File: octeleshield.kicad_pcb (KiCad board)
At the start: 2 copper layers, 30 parts, among them P1 POWER_HEADER, P10 THERMOCOUPLE1, P11 THERMOCOUPLE2, P2 ANALOG_HEADER, P3 ICSP_HEADER, P4 DIGITAL_HEADER_2, P5 DIGITAL_HEADER_1, P6 V_PROBE2_SIG, P7 V_PROBE2_GND, P8 V_PROBE1_SIG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

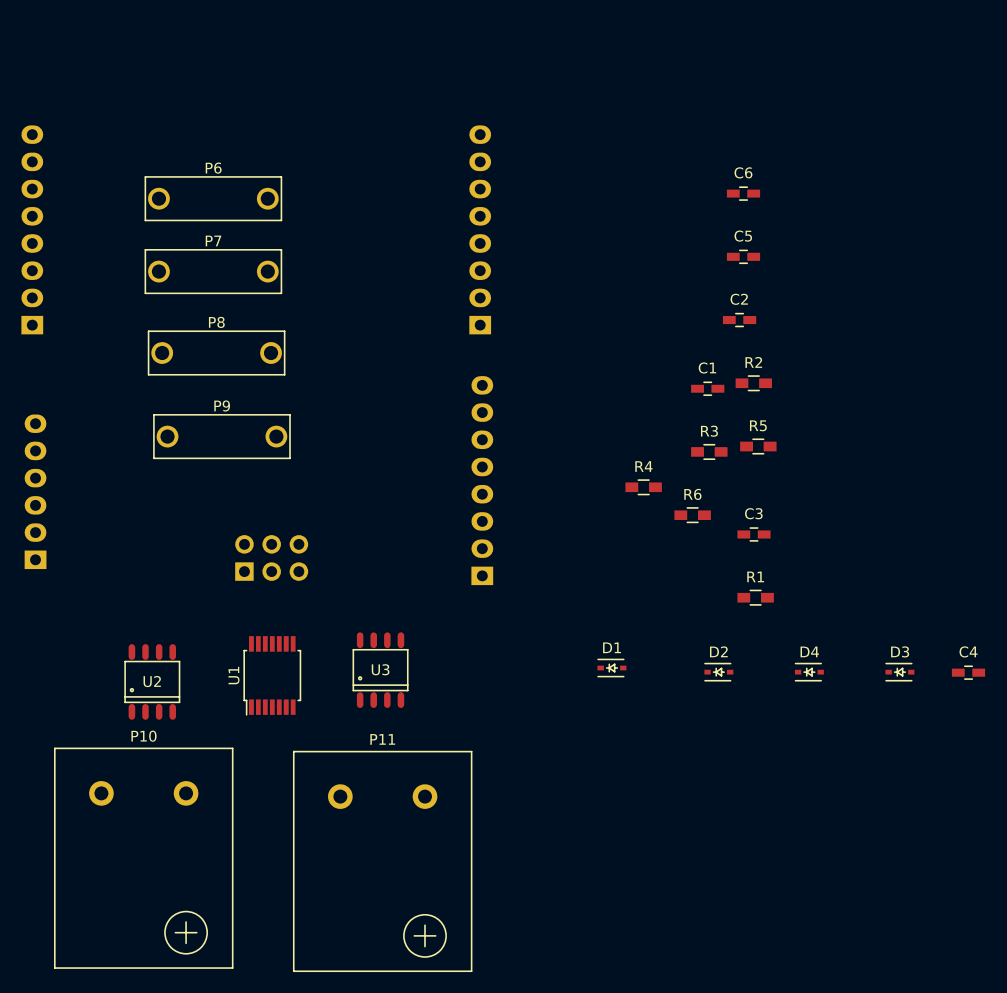
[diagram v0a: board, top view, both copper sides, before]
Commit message: work in progress, first try of pcb layout
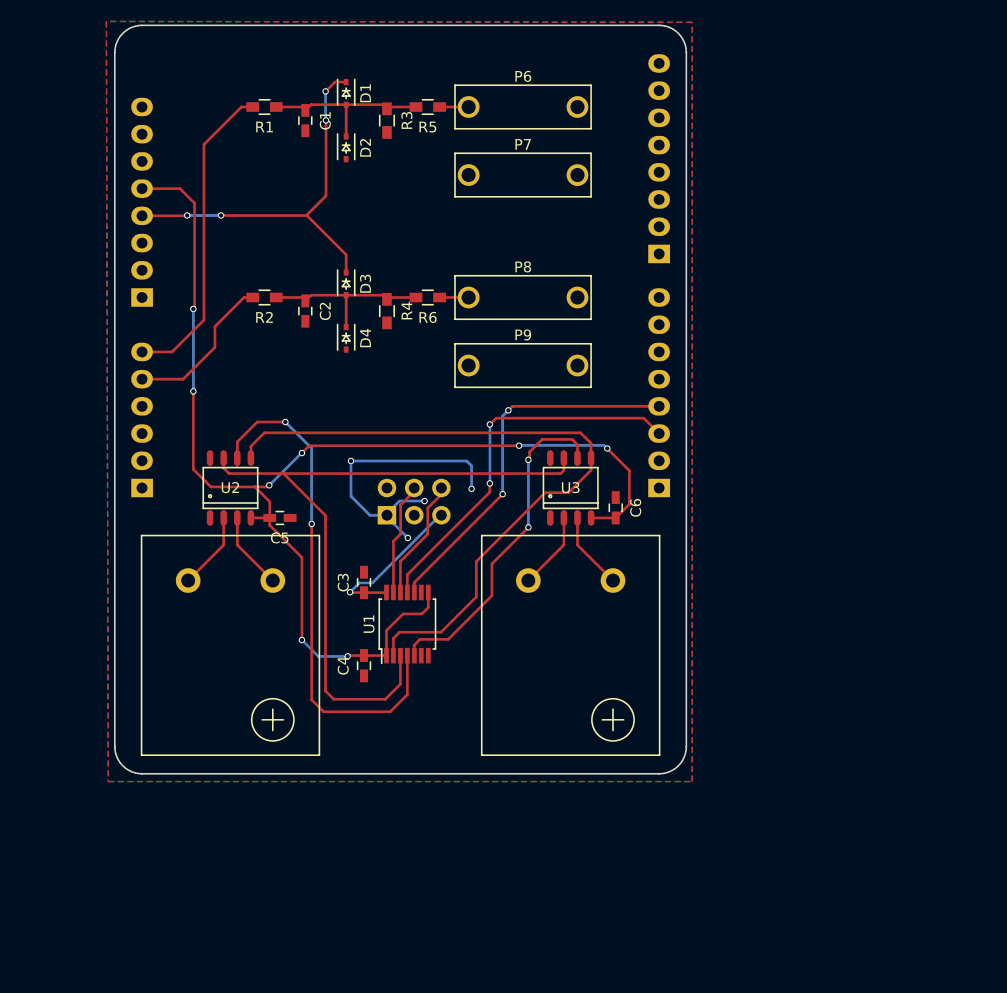
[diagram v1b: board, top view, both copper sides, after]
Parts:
- moved R1 64.8 mm to (115.6, 66.0), turned to 180 degrees
- moved D3 63.1 mm to (123.2, 82.5), turned to 270 degrees
- moved D2 60.0 mm to (123.2, 69.8), turned to 270 degrees
- moved D1 59.1 mm to (123.2, 64.8), turned to 270 degrees
- moved C4 56.4 mm to (124.9, 118.2), turned to 90 degrees
- moved D4 53.3 mm to (123.2, 87.6), turned to 270 degrees
- moved C5 49.7 mm to (117.0, 104.4), turned to 180 degrees
- moved R2 46.4 mm to (115.6, 83.8), turned to 180 degrees
- moved C1 45.1 mm to (119.4, 67.3), turned to 270 degrees
- moved R5 44.2 mm to (130.8, 66.0), turned to 180 degrees
- moved R3 43.1 mm to (127.0, 67.3), turned to 270 degrees
- moved C2 40.5 mm to (119.4, 85.1), turned to 270 degrees
- moved C3 36.7 mm to (124.9, 110.4), turned to 90 degrees
- moved R6 32.0 mm to (130.8, 83.8), turned to 180 degrees
- moved C6 31.7 mm to (148.4, 103.4), turned to 270 degrees
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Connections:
- P2 pad 1: /A0 -> Net-(P2-Pad1)
- P2 pad 2: /A1 -> Net-(P2-Pad2)
- P2 pad 5: Net-(P2-Pad5) -> /A4
- P2 pad 6: Net-(P2-Pad6) -> /A5
- P5 pad 3: Net-(P5-Pad3) -> /CS1
- P5 pad 4: Net-(P5-Pad4) -> /CS2
- P5 pad 5: /TC_ENABLE -> Net-(P5-Pad5)
- P5 pad 6: /CS1 -> Net-(P5-Pad6)
- P5 pad 7: /CS2 -> Net-(P5-Pad7)
- R1 pad 2: /A1 -> /A5
- R2 pad 2: /A0 -> /A4
- U1 pad 8: /TC_ENABLE -> +3V3
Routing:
- net +3V3: track 0.00 -> 116.5 mm, vias 0 -> 8
- net Net-(U1-Pad3): track 0.00 -> 66.6 mm
- net Net-(U1-Pad2): track 0.00 -> 64.8 mm
- net +5V: track 0.00 -> 51.8 mm, vias 0 -> 5
- net Net-(U1-Pad4): track 0.00 -> 48.1 mm, vias 0 -> 2
- net /CS1: track 0.00 -> 35.5 mm, vias 0 -> 2
- net /CS2: track 0.00 -> 34.9 mm, vias 0 -> 2
- net Net-(U1-Pad5): track 0.00 -> 31.4 mm, vias 0 -> 2
- net /A5: track 0.00 -> 29.4 mm
- net GND: track 0.00 -> 28.1 mm, vias 0 -> 4
- net Net-(C2-Pad1): track 0.00 -> 16.6 mm
- net Net-(C1-Pad1): track 0.00 -> 16.6 mm
- net /A4: track 0.00 -> 14.6 mm
- net /MISO: track 0.00 -> 12.6 mm
- net /SCLK: track 0.00 -> 11.1 mm
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- added copper zone on B.Cu, net GND
- added copper zone on F.Cu, net GND
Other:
- board outline added: 53.3 x 69.9 mm

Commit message: work in progress, component updates
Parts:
- C1, C2: value 10n -> 100n
- C3, C4, C5, C6: value 0.1u -> 100n
- R5, R6: value 33.2k -> 33k
- U2, U3: value MAX31855KASA -> MAX31855KASA+
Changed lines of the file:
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@@
-(kicad_pcb (version 4) (host pcbnew 4.0.1-stable)
+(kicad_pcb (version 4) (host pcbnew 4.0.2-stable)
   (general
     (links 57)
@@
   (title_block
     (title "Overclocking telemetry shield for Arduino Yún")
-    (date 2016-01-17)
+    (date 2016-02-22)
     (rev v1)
     (company Moonpunch.org)
@@
       (effects (font (size 1 1) (thickness 0.15)))
     )
-    (fp_text value 10n (at 0 1.9 270) (layer F.Fab)
+    (fp_text value 100n (at 0 1.9 270) (layer F.Fab)
       (effects (font (size 1 1) (thickness 0.15)))
     )
@@
       (effects (font (size 1 1) (thickness 0.15)))
     )
-    (fp_text value 10n (at 0 1.9 270) (layer F.Fab)
+    (fp_text value 100n (at 0 1.9 270) (layer F.Fab)
       (effects (font (size 1 1) (thickness 0.15)))
     )
@@
       (effects (font (size 1 1) (thickness 0.15)))
     )
-    (fp_text value 0.1u (at 0 1.9 90) (layer F.Fab)
+    (fp_text value 100n (at 0 1.9 90) (layer F.Fab)
       (effects (font (size 1 1) (thickness 0.15)))
     )
@@
       (effects (font (size 1 1) (thickness 0.15)))
     )
-    (fp_text value 0.1u (at 0 1.9 90) (layer F.Fab)
+    (fp_text value 100n (at 0 1.9 90) (layer F.Fab)
       (effects (font (size 1 1) (thickness 0.15)))
     )
@@
       (effects (font (size 1 1) (thickness 0.15)))
     )
-    (fp_text value 0.1u (at 0 1.9 180) (layer F.Fab)
+    (fp_text value 100n (at 0 1.9 180) (layer F.Fab)
       (effects (font (size 1 1) (thickness 0.15)))
     )
@@
       (effects (font (size 1 1) (thickness 0.15)))
     )
-    (fp_text value 0.1u (at 0 1.9 270) (layer F.Fab)
+    (fp_text value 100n (at 0 1.9 270) (layer F.Fab)
       (effects (font (size 1 1) (thickness 0.15)))
     )
@@
       (effects (font (size 1 1) (thickness 0.15)))
     )
-    (fp_text value 33.2k (at 0 1.9 180) (layer F.Fab)
+    (fp_text value 33k (at 0 1.9 180) (layer F.Fab)
       (effects (font (size 1 1) (thickness 0.15)))
     )
@@
       (effects (font (size 1 1) (thickness 0.15)))
     )
-    (fp_text value 33.2k (at 0 1.9 180) (layer F.Fab)
+    (fp_text value 33k (at 0 1.9 180) (layer F.Fab)
       (effects (font (size 1 1) (thickness 0.15)))
     )
@@
       (effects (font (size 1 1) (thickness 0.15)))
     )
-    (fp_text value MAX31855KASA (at 0 0) (layer F.Fab)
+    (fp_text value MAX31855KASA+ (at 0 0) (layer F.Fab)
       (effects (font (size 1 1) (thickness 0.15)))
     )
@@
       (effects (font (size 1 1) (thickness 0.15)))
     )
-    (fp_text value MAX31855KASA (at 0 0) (layer F.Fab)
+    (fp_text value MAX31855KASA+ (at 0 0) (layer F.Fab)
       (effects (font (size 1 1) (thickness 0.15)))
     )
@@
       (effects (font (size 1 1) (thickness 0.15)))
     )
-    (fp_text value THERMOCOUPLE1 (at 0.05 17.3) (layer F.Fab)
+    (fp_text value THERMOCOUPLE1 (at 0.05 17.3) (layer F.SilkS)
       (effects (font (size 1 1) (thickness 0.15)))
     )
@@
       (effects (font (size 1 1) (thickness 0.15)))
     )
-    (fp_text value THERMOCOUPLE2 (at 0.05 17.3) (layer F.Fab)
-      (effects (font (size 1 1) (thickness 0.15)))
-    )
+    (fp_text value THERMOCOUPLE2 (at 0.05 17.3) (layer F.SilkS)
+      (effects (font (size 1 1) (thickness 0.15)))
+    )

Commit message: more work in progress, getting there
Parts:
- added G***: MOONPUNCH_LOGO, parts:moonpunch_1cm, F.Cu at (108.5, 61.5)
- added G***: LOGO, parts:epeak_logo, F.Cu at (122.8, 95.1)
- P10: value THERMOCOUPLE1 -> THERMOCOUPLE1/D3
- P11: value THERMOCOUPLE2 -> THERMOCOUPLE2/D4
- P6: value V_PROBE2_SIG -> V_PROBE1_SIG
- P7: value V_PROBE2_GND -> V_PROBE1_GND
- P8: value V_PROBE1_SIG -> V_PROBE2_SIG
- P9: value V_PROBE1_GND -> V_PROBE2_GND
- U2, U3: value MAX31855KASA+ -> MAX31855
- moved P10 1.00 mm to (112.4, 111.2)
- moved P11 1.00 mm to (144.1, 111.2)
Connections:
- net /A4 renamed /A1
- net /A5 renamed /A0
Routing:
- net Net-(P11-Pad2): track 7.22 -> 8.22 mm
- net Net-(P11-Pad1): track 7.22 -> 8.22 mm
- net Net-(P10-Pad1): track 7.22 -> 8.22 mm
- net Net-(P10-Pad2): track 7.22 -> 8.22 mm
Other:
- board text added: "Designed in Taiwan 2016-02-24"
- board text added: "EPEAK GEARS"
- board text added: "Overclocking Telemetry Shield"
- board text added: "Voltage1/A0"
- board text added: "Voltage2/A1"
- board text added: "moonpunch.org"
- board text added: "v1"

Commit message: PCB modifications
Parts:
- moved C6 1.43 mm to (149.5, 104.4), turned to 180 degrees
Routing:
- net +3V3: track 116.5 -> 115.5 mm
- net Net-(U1-Pad4): track 48.1 -> 49.1 mm
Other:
- board text added: "Designed in Taiwan 2016-03-01"
- board text added: "rev0"
- board text removed: "Designed in Taiwan 2016-02-24"
- board text removed: "v1"
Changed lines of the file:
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@@
     (visible_elements FFFFE77F)
     (pcbplotparams
-      (layerselection 0x020f0_80000001)
-      (usegerberextensions false)
+      (layerselection 0x010f0_80000001)
+      (usegerberextensions true)
       (excludeedgelayer true)
       (linewidth 0.100000)
@@
   )
   (module Capacitors_SMD:C_0603_HandSoldering (layer F.Cu)
-    (at 148.35124 103.44404 270)
+    (at 149.45106 104.3559 180)
     (descr "Capacitor SMD 0603, hand soldering")
     (tags "capacitor 0603")
     (attr smd)
-    (fp_text reference C6 (at 1.27508 -1.68656 270) (layer F.SilkS)
-      (effects (font (size 1 1) (thickness 0.15)))
-    )
-    (fp_text value 100n (at -2.35712 -1.68656 270) (layer F.SilkS)
+    (fp_text reference C6 (at 1.00584 1.397 180) (layer F.SilkS)
+      (effects (font (size 1 1) (thickness 0.15)))
+    )
+    (fp_text value 100n (at 0.11176 -1.397 180) (layer F.SilkS)
       (effects (font (size 1 1) (thickness 0.15)))
     )
@@
     (fp_line (start -0.35 -0.6) (end 0.35 -0.6) (layer F.SilkS) (width 0.15))
     (fp_line (start 0.35 0.6) (end -0.35 0.6) (layer F.SilkS) (width 0.15))
-    (pad 1 smd rect (at -0.95 0 270) (size 1.2 0.75) (layers F.Cu F.Paste F.Mask)
+    (pad 1 smd rect (at -0.95 0 180) (size 1.2 0.75) (layers F.Cu F.Paste F.Mask)
       (net 2 GND))
-    (pad 2 smd rect (at 0.95 0 270) (size 1.2 0.75) (layers F.Cu F.Paste F.Mask)
+    (pad 2 smd rect (at 0.95 0 180) (size 1.2 0.75) (layers F.Cu F.Paste F.Mask)
       (net 5 +3V3))
     (model Capacitors_SMD.3dshapes/C_0603_HandSoldering.wrl
@@
     (pad "" np_thru_hole circle (at 0 10.25) (size 2.6 2.6) (drill 2.6) (layers *.Cu *.Mask F.SilkS))
   )
-  (gr_text "Designed in Taiwan\n2016-02-24" (at 114.554 62.25032) (layer B.SilkS)
+  (gr_text "Designed in Taiwan\n2016-03-01" (at 114.554 62.25032) (layer B.SilkS)
     (effects (font (size 1.5 1.5) (thickness 0.3)) (justify mirror))
   )
-  (gr_text v1 (at 133.60908 126.67996) (layer F.SilkS)
+  (gr_text rev0 (at 133.79704 126.7714) (layer F.SilkS)
     (effects (font (size 1.016 1.016) (thickness 0.1524)))
   )
@@
   (segment (start 126.9412 111.3638) (end 126.955 111.35) (width 0.25) (layer F.Cu) (net 4))
   (segment (start 132.08 104.14) (end 132.06476 104.14) (width 0.25) (layer B.Cu) (net 4))
+  (segment (start 148.3512 104.394) (end 148.35124 104.39404) (width 0.25) (layer F.Cu) (net 5))
+  (via (at 147.56384 97.917) (size 0.6) (drill 0.4) (layers F.Cu B.Cu) (net 5))
+  (segment (start 147.56384 97.917) (end 148.39188 98.74504) (width 0.25) (layer F.Cu) (net 5))
+  (segment (start 148.39188 98.74504) (end 148.39188 104.3534) (width 0.25) (layer F.Cu) (net 5))
+  (segment (start 148.39188 104.3534) (end 148.35124 104.39404) (width 0.25) (layer F.Cu) (net 5))
+  (segment (start 147.25904 97.6122) (end 147.56384 97.917) (width 0.25) (layer B.Cu) (net 5))
+  (segment (start 119.75084 97.65284) (end 139.33424 97.65284) (width 0.25) (layer F.Cu) (net 5))
+  (via (at 139.33424 97.65284) (size 0.6) (drill 0.4) (layers F.Cu B.Cu) (net 5))
+  (segment (start 139.33424 97.65284) (end 139.37488 97.6122) (width 0.25) (layer B.Cu) (net 5))
+  (segment (start 139.37488 97.6122) (end 147.25904 97.6122) (width 0.25) (layer B.Cu) (net 5))
   (segment (start 114.681 101.4984) (end 115.86464 101.4984) (width 0.25) (layer F.Cu) (net 5))
-  (segment (start 149.62124 103.12404) (end 148.35124 104.39404) (width 0.25) (layer F.Cu) (net 5))
-  (segment (start 149.62124 99.9744) (end 149.62124 103.12404) (width 0.25) (layer F.Cu) (net 5))
-  (segment (start 147.56384 97.917) (end 149.62124 99.9744) (width 0.25) (layer F.Cu) (net 5))
-  (via (at 147.56384 97.917) (size 0.6) (drill 0.4) (layers F.Cu B.Cu) (net 5))
-  (segment (start 147.25904 97.6122) (end 147.56384 97.917) (width 0.25) (layer B.Cu) (net 5))
-  (segment (start 139.37488 97.6122) (end 147.25904 97.6122) (width 0.25) (layer B.Cu) (net 5))
-  (segment (start 139.33424 97.65284) (end 139.37488 97.6122) (width 0.25) (layer B.Cu) (net 5))
-  (via (at 139.33424 97.65284) (size 0.6) (drill 0.4) (layers F.Cu B.Cu) (net 5))
-  (segment (start 119.75084 97.65284) (end 139.33424 97.65284) (width 0.25) (layer F.Cu) (net 5))
+  (segment (start 146.05 104.394) (end 148.3512 104.394) (width 0.25) (layer F.Cu) (net 5))
+  (segment (start 115.86464 101.4984) (end 116.01704 101.346) (width 0.25) (layer F.Cu) (net 5))
+  (via (at 116.01704 101.346) (size 0.6) (drill 0.4) (layers F.Cu B.Cu) (net 5))
+  (segment (start 116.01704 101.346) (end 119.0244 98.33864) (width 0.25) (layer B.Cu) (net 5))
+  (segment (start 119.0244 98.33864) (end 119.06504 98.33864) (width 0.25) (layer B.Cu) (net 5))
+  (via (at 119.06504 98.33864) (size 0.6) (drill 0.4) (layers F.Cu B.Cu) (net 5))
   (segment (start 119.06504 98.33864) (end 119.75084 97.65284) (width 0.25) (layer F.Cu) (net 5))
-  (via (at 119.06504 98.33864) (size 0.6) (drill 0.4) (layers F.Cu B.Cu) (net 5))
-  (segment (start 119.0244 98.33864) (end 119.06504 98.33864) (width 0.25) (layer B.Cu) (net 5))
-  (segment (start 116.01704 101.346) (end 119.0244 98.33864) (width 0.25) (layer B.Cu) (net 5))
-  (via (at 116.01704 101.346) (size 0.6) (drill 0.4) (layers F.Cu B.Cu) (net 5))
-  (segment (start 115.86464 101.4984) (end 116.01704 101.346) (width 0.25) (layer F.Cu) (net 5))
   (segment (start 116.05764 104.394) (end 116.05764 105.08484) (width 0.25) (layer F.Cu) (net 5))
   (segment (start 123.40848 117.2362) (end 124.85624 117.2362) (width 0.25) (layer F.Cu) (net 5))
@@
   (segment (start 114.681 101.4984) (end 110.5662 101.4984) (width 0.25) (layer F.Cu) (net 5))
   (segment (start 116.05764 102.87504) (end 114.681 101.4984) (width 0.25) (layer F.Cu) (net 5))
-  (segment (start 146.05 104.394) (end 148.3512 104.394) (width 0.25) (layer F.Cu) (net 5))
-  (segment (start 148.3512 104.394) (end 148.35124 104.39404) (width 0.25) (layer F.Cu) (net 5))
   (segment (start 126.955 117.25) (end 126.955 114.9038) (width 0.25) (layer F.Cu) (net 5))
   (segment (start 130.855 112.7564) (end 130.855 111.35) (width 0.25) (layer F.Cu) (net 5))
@@
   (segment (start 146.05 98.806) (end 146.05 99.93376) (width 0.25) (layer F.Cu) (net 34))
   (segment (start 127.605 115.64064) (end 127.605 117.25) (width 0.25) (layer F.Cu) (net 34))
-  (segment (start 128.18872 115.05692) (end 127.605 115.64064) (width 0.25) (layer F.Cu) (net 34))
-  (segment (start 132.04444 115.05692) (end 128.18872 115.05692) (width 0.25) (layer F.Cu) (net 34))
-  (segment (start 135.34136 111.76) (end 132.04444 115.05692) (width 0.25) (layer F.Cu) (net 34))
-  (segment (start 135.34136 108.46308) (end 135.34136 111.76) (width 0.25) (layer F.Cu) (net 34))
+  (segment (start 128.83134 114.4143) (end 127.605 115.64064) (width 0.25) (layer F.Cu) (net 34))
+  (segment (start 131.98856 114.4143) (end 128.83134 114.4143) (width 0.25) (layer F.Cu) (net 34))
+  (segment (start 135.34136 111.0615) (end 131.98856 114.4143) (width 0.25) (layer F.Cu) (net 34))
+  (segment (start 135.34136 108.46308) (end 135.34136 111.0615) (width 0.25) (layer F.Cu) (net 34))
   (segment (start 141.76756 102.03688) (end 135.34136 108.46308) (width 0.25) (layer F.Cu) (net 34))
   (segment (start 143.94688 102.03688) (end 141.76756 102.03688) (width 0.25) (layer F.Cu) (net 34))
@@
   (segment (start 117.348 100.24872) (end 112.26292 100.24872) (width 0.25) (layer F.Cu) (net 35))
   (segment (start 143.51 99.95916) (end 143.22044 100.24872) (width 0.25) (layer F.Cu) (net 35))
-  (segment (start 113.03 98.806) (end 113.03 97.30232) (width 0.25) (layer F.Cu) (net 36))
+  (segment (start 113.03 98.806) (end 113.03 96.32696) (width 0.25) (layer F.Cu) (net 36))
   (segment (start 128.905 120.8786) (end 128.905 117.25) (width 0.25) (layer F.Cu) (net 36))
   (segment (start 127.29464 122.48896) (end 128.905 120.8786) (width 0.25) (layer F.Cu) (net 36))
@@
   (via (at 119.97436 104.94264) (size 0.6) (drill 0.4) (layers F.Cu B.Cu) (net 36))
   (segment (start 119.97436 97.90176) (end 119.97436 104.94264) (width 0.25) (layer B.Cu) (net 36))
-  (segment (start 117.51564 95.44304) (end 119.97436 97.90176) (width 0.25) (layer B.Cu) (net 36))
-  (via (at 117.51564 95.44304) (size 0.6) (drill 0.4) (layers F.Cu B.Cu) (net 36))
-  (segment (start 114.88928 95.44304) (end 117.51564 95.44304) (width 0.25) (layer F.Cu) (net 36))
-  (segment (start 113.03 97.30232) (end 114.88928 95.44304) (width 0.25) (layer F.Cu) (net 36))
+  (segment (start 116.56568 94.82836) (end 119.97436 97.90176) (width 0.25) (layer B.Cu) (net 36))
+  (via (at 116.56568 94.82836) (size 0.6) (drill 0.4) (layers F.Cu B.Cu) (net 36))
+  (segment (start 114.47018 94.8563) (end 116.56568 94.82836) (width 0.25) (layer F.Cu) (net 36))
+  (segment (start 113.03 96.32696) (end 114.47018 94.8563) (width 0.25) (layer F.Cu) (net 36))
   (segment (start 113.03 99.50704) (end 113.03 98.806) (width 0.25) (layer F.Cu) (net 36))
   (segment (start 129.555 117.25) (end 129.555 116.26112) (width 0.25) (layer F.Cu) (net 37))
